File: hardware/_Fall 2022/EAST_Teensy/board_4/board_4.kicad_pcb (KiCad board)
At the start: 2 copper layers, 76.2 x 66.7 mm, 11 parts, among them J1 Conn_01x04, J2 Conn_02x09_Odd_Even, U1 Teensy4.1

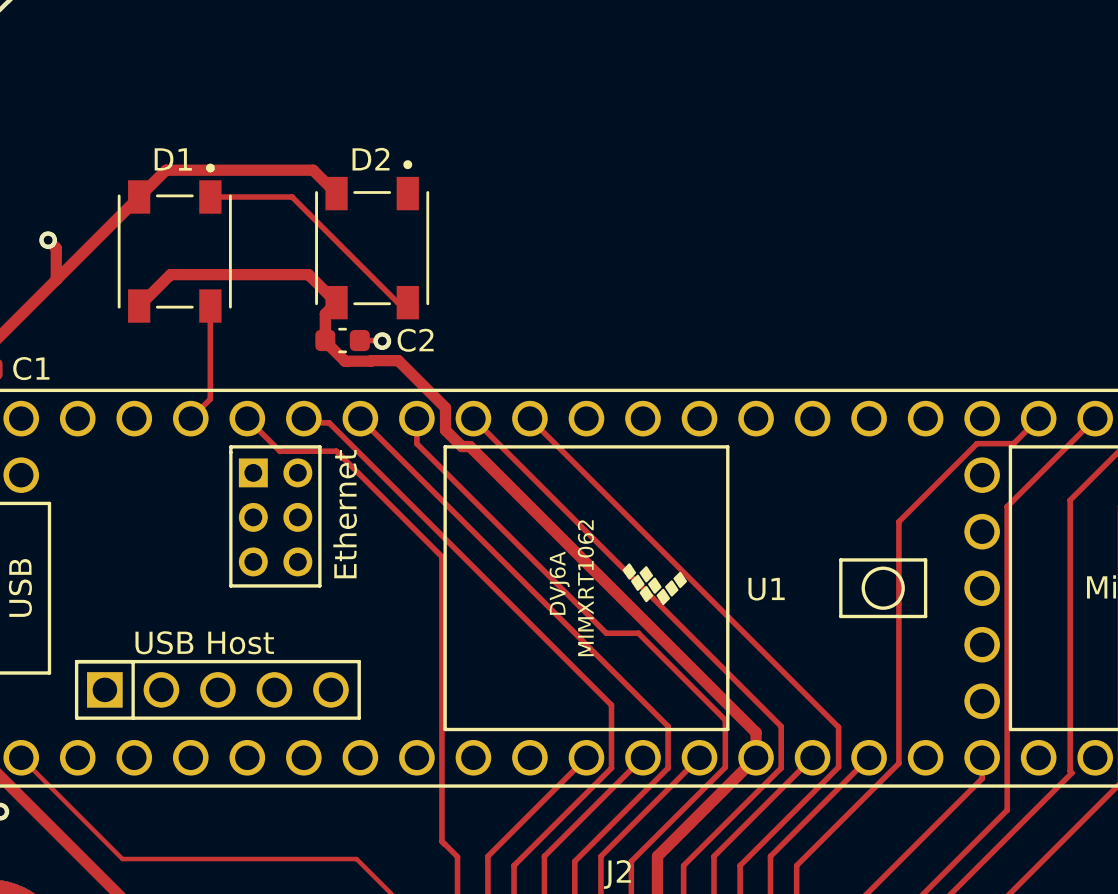
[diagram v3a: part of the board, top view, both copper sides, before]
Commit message: Edit for design rule check
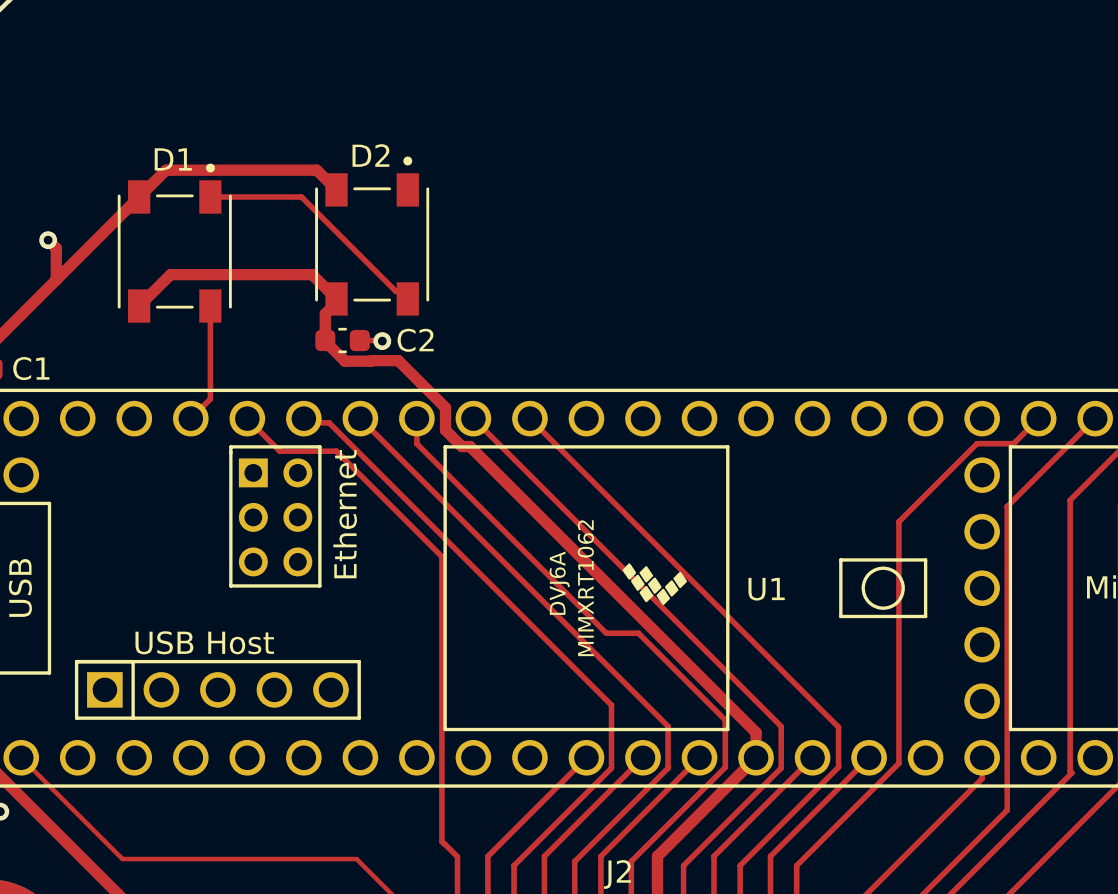
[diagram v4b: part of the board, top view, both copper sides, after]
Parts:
- moved D2 0.16 mm to (137.7, 107.2)
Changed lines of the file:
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@@
       (effects (font (size 1 1) (thickness 0.15)))
     )
-    (fp_text value "0.1uf" (at 0 1.43 180) (layer "F.Fab")
+    (fp_text value "0.1uf" (at 0 1.59495 180) (layer "F.Fab")
       (effects (font (size 1 1) (thickness 0.15)))
     )
@@
   )
   (footprint "Neopixel:LED_1655" (layer "F.Cu")
-    (at 137.72 107.3275 -90)
+    (at 137.72 107.16255 -90)
     (property "Sheetfile" "board_4.kicad_sch")
     (property "Sheetname" "")
@@
   (segment (start 137.84 140.68) (end 144.48 147.32) (width 0.508) (layer "F.Cu") (net 1))
   (segment (start 144.48 147.32) (end 161.798 147.32) (width 0.508) (layer "F.Cu") (net 1))
-  (segment (start 136.12 104.8775) (end 135.0685 103.826) (width 0.508) (layer "F.Cu") (net 2))
   (segment (start 123.525 107.335) (end 123.16 106.97) (width 0.508) (layer "F.Cu") (net 2))
+  (segment (start 135.23345 103.826) (end 136.12 104.71255) (width 0.508) (layer "F.Cu") (net 2))
   (segment (start 138.15 111.48) (end 138.176 111.506) (width 0.25) (layer "F.Cu") (net 2))
   (segment (start 137.84 138.14) (end 134.6 138.14) (width 0.508) (layer "F.Cu") (net 2))
-  (segment (start 128.454 103.826) (end 127.25 105.03) (width 0.508) (layer "F.Cu") (net 2))
   (segment (start 119.41 130.23) (end 119.41 131.05) (width 0.381) (layer "F.Cu") (net 2))
   (segment (start 134.6 138.14) (end 134.32 137.86) (width 0.508) (layer "F.Cu") (net 2))
   (segment (start 120.589 111.691) (end 120.589 112.845526) (width 0.508) (layer "F.Cu") (net 2))
-  (segment (start 135.0685 103.826) (end 128.454 103.826) (width 0.508) (layer "F.Cu") (net 2))
+  (segment (start 127.25 105.03) (end 128.454 103.826) (width 0.508) (layer "F.Cu") (net 2))
   (segment (start 123.525 108.755) (end 120.589 111.691) (width 0.508) (layer "F.Cu") (net 2))
   (segment (start 127.25 105.03) (end 123.525 108.755) (width 0.508) (layer "F.Cu") (net 2))
   (segment (start 137.165 111.48) (end 138.15 111.48) (width 0.25) (layer "F.Cu") (net 2))
   (segment (start 119.41 131.05) (end 121.01 132.65) (width 0.381) (layer "F.Cu") (net 2))
+  (segment (start 128.454 103.826) (end 135.23345 103.826) (width 0.508) (layer "F.Cu") (net 2))
   (segment (start 123.525 108.755) (end 123.525 107.335) (width 0.508) (layer "F.Cu") (net 2))
   (via (at 134.32 137.86) (size 0.8) (drill 0.4) (layers "F.Cu" "B.Cu") (net 2))
@@
   (via (at 138.176 111.506) (size 0.8) (drill 0.4) (layers "F.Cu" "B.Cu") (net 2))
   (via (at 123.16 106.97) (size 0.8) (drill 0.4) (layers "F.Cu" "B.Cu") (net 2))
-  (segment (start 130.45 105.03) (end 134.12 105.03) (width 0.25) (layer "F.Cu") (net 3))
-  (segment (start 134.12 105.03) (end 138.8675 109.7775) (width 0.25) (layer "F.Cu") (net 3))
-  (segment (start 138.8675 109.7775) (end 139.32 109.7775) (width 0.25) (layer "F.Cu") (net 3))
+  (segment (start 138.97825 109.2708) (end 139.32 109.61255) (width 0.25) (layer "F.Cu") (net 3))
+  (segment (start 130.45 105.03) (end 134.5448 105.03) (width 0.25) (layer "F.Cu") (net 3))
+  (segment (start 134.5448 105.03) (end 138.7856 109.2708) (width 0.25) (layer "F.Cu") (net 3))
+  (segment (start 138.7856 109.2708) (end 138.97825 109.2708) (width 0.25) (layer "F.Cu") (net 3))
   (segment (start 175.29 114.99) (end 171.3484 118.9316) (width 0.25) (layer "F.Cu") (net 4))
   (segment (start 171.3484 131.3688) (end 162.29 140.4272) (width 0.25) (layer "F.Cu") (net 4))
@@
   (segment (start 161.365 138.7106) (end 161.365 142.2014) (width 0.25) (layer "F.Cu") (net 5))
   (segment (start 169.164 130.9116) (end 161.365 138.7106) (width 0.25) (layer "F.Cu") (net 5))
-  (segment (start 134.862 108.5195) (end 128.6605 108.5195) (width 0.508) (layer "F.Cu") (net 6))
   (segment (start 137.671251 112.409) (end 136.501 112.409) (width 0.508) (layer "F.Cu") (net 6))
-  (segment (start 136.12 109.7775) (end 134.862 108.5195) (width 0.508) (layer "F.Cu") (net 6))
+  (segment (start 135.02695 108.5195) (end 136.12 109.61255) (width 0.508) (layer "F.Cu") (net 6))
   (segment (start 141.750576 116.244) (end 141.016 115.509424) (width 0.508) (layer "F.Cu") (net 6))
   (segment (start 150.54 138.14) (end 150.54 134.66) (width 0.508) (layer "F.Cu") (net 6))
   (segment (start 138.897424 112.384) (end 137.696251 112.384) (width 0.508) (layer "F.Cu") (net 6))
+  (segment (start 127.25 109.93) (end 128.6605 108.5195) (width 0.508) (layer "F.Cu") (net 6))
   (segment (start 141.016 114.502576) (end 138.897424 112.384) (width 0.508) (layer "F.Cu") (net 6))
   (segment (start 154.97 129.09863) (end 142.11537 116.244) (width 0.508) (layer "F.Cu") (net 6))
+  (segment (start 128.6605 108.5195) (end 135.02695 108.5195) (width 0.508) (layer "F.Cu") (net 6))
   (segment (start 154.97 130.23) (end 154.97 129.09863) (width 0.508) (layer "F.Cu") (net 6))
+  (segment (start 136.12 109.61255) (end 136.12 109.7775) (width 0.508) (layer "F.Cu") (net 6))
   (segment (start 142.11537 116.244) (end 141.750576 116.244) (width 0.508) (layer "F.Cu") (net 6))
   (segment (start 136.501 112.409) (end 135.615 111.523) (width 0.508) (layer "F.Cu") (net 6))
-  (segment (start 128.6605 108.5195) (end 127.25 109.93) (width 0.508) (layer "F.Cu") (net 6))
   (segment (start 141.016 115.509424) (end 141.016 114.502576) (width 0.508) (layer "F.Cu") (net 6))
   (segment (start 150.54 134.66) (end 154.97 130.23) (width 0.508) (layer "F.Cu") (net 6))
@@
   (segment (start 158.16 138.14) (end 165.13 131.17) (width 0.25) (layer "F.Cu") (net 9))
   (segment (start 165.13 131.17) (end 165.13 130.23) (width 0.25) (layer "F.Cu") (net 9))
-  (segment (start 164.64 130.23) (end 165.13 130.23) (width 0.25) (layer "F.Cu") (net 9))
   (segment (start 126.5 134.78) (end 137.02 134.78) (width 0.2032) (layer "F.Cu") (net 10))
   (segment (start 137.02 134.78) (end 140.38 138.14) (width 0.2032) (layer "F.Cu") (net 10))

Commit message: EAST JLC files
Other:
- board text added: "Ari Bobesh Charlie Babe Jiayuan Liu Lili Baker Rowan Jansens"
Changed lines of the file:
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@@
       (outputformat 1)
       (mirror false)
-      (drillshape 1)
+      (drillshape 0)
       (scaleselection 1)
-      (outputdirectory "")
+      (outputdirectory "JLC/")
     )
   )
@@
     (tags "mounting hole 3.7mm")
     (attr exclude_from_pos_files exclude_from_bom)
-    (fp_text reference "REF**" (at 10.414 1.27) (layer "F.SilkS")
+    (fp_text reference "REF**" (at 10.414 1.27) (layer "F.SilkS") hide
       (effects (font (size 1 1) (thickness 0.15)))
     )
@@
     (tags "mounting hole 3.7mm")
     (attr exclude_from_pos_files exclude_from_bom)
-    (fp_text reference "REF**" (at -0.656228 -9.486125) (layer "F.SilkS")
+    (fp_text reference "REF**" (at -0.656228 -9.486125) (layer "F.SilkS") hide
       (effects (font (size 1 1) (thickness 0.15)))
     )
@@
     (tags "mounting hole 3.7mm")
     (attr exclude_from_pos_files exclude_from_bom)
-    (fp_text reference "REF**" (at -9.228277 3.101257) (layer "F.SilkS")
+    (fp_text reference "REF**" (at -9.228277 3.101257) (layer "F.SilkS") hide
       (effects (font (size 1 1) (thickness 0.15)))
     )
@@
     (fp_line (start 0.5 1.375) (end 0 0.875) (layer "F.Fab") (width 0.1))
     (fp_line (start 7.25 0.25) (end -1.25 0.25) (layer "F.Fab") (width 0.1))
-    (pad "1" thru_hole roundrect (at 0 0) (size 1.2 1.75) (drill 0.75) (layers *.Cu *.Mask) (roundrect_rratio 0.208333)
+    (pad "1" thru_hole roundrect (at 0 0) (size 1.2 1.75) (drill 0.75) (layers *.Cu *.Mask) (roundrect_rratio 0.2083333333)
       (net 5 "/TX 0") (pinfunction "Pin_1") (pintype "passive"))
     (pad "2" thru_hole oval (at 2 0) (size 1.2 1.75) (drill 0.75) (layers *.Cu *.Mask)
@@
   (gr_line (start 122.779619 152.0952) (end 173.181181 152.0952) (layer "Edge.Cuts") (width 0.2))
   (gr_arc (start 122.779619 152.0952) (mid 147.9804 85.403268) (end 173.181181 152.0952) (layer "Edge.Cuts") (width 0.2))
+  (gr_text "Ari Bobesh\nCharlie Babe\nJiayuan Liu\nLili Baker\nRowan Jansens" (at 147.8788 104.4956) (layer "B.SilkS")
+    (effects (font (size 2 2) (thickness 0.15)) (justify mirror))
+  )
   (segment (start 137.84 140.68) (end 130.626576 140.68) (width 0.508) (layer "F.Cu") (net 1))
   (segment (start 120.671646 125.972938) (end 118.85 124.151292) (width 0.508) (layer "F.Cu") (net 1))

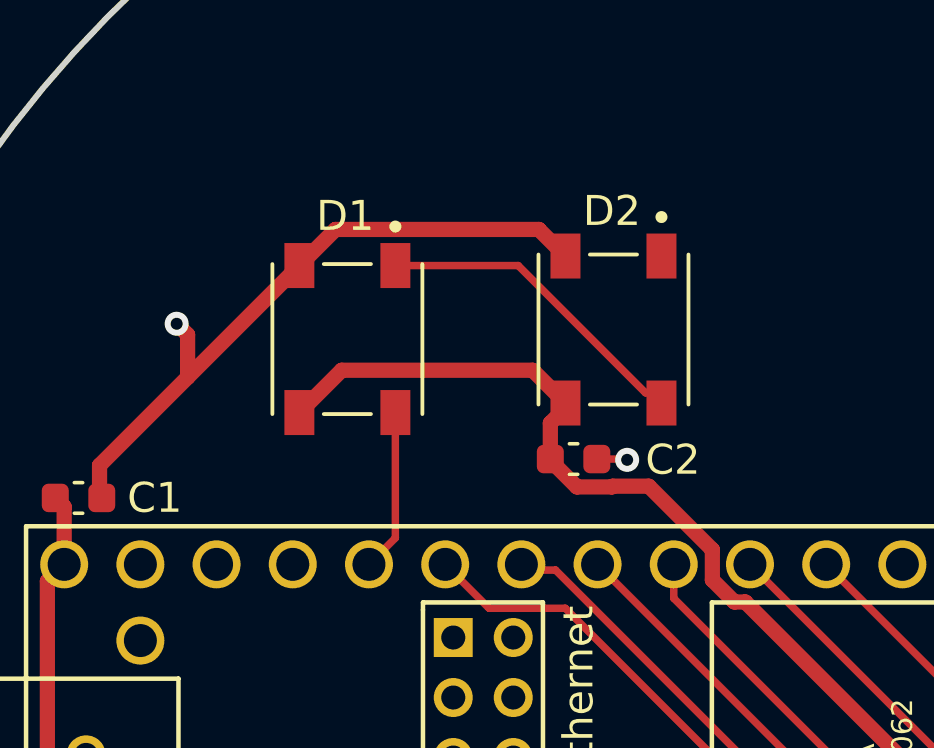
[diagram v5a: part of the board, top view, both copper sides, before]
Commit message: Changed neopixel on board 4
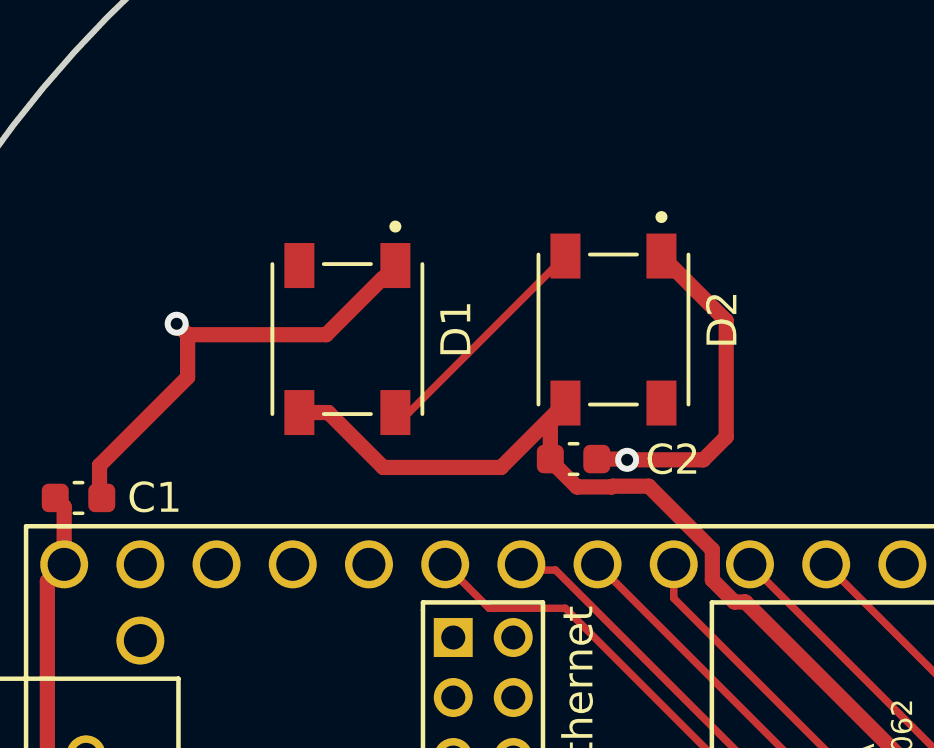
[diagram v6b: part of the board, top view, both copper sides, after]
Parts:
- D1: value Neopixel1 -> 1655; footprint Neopixel:LED_1655 -> neopixel:LED_1655
- D2: value Neopixel2 -> 1655; footprint Neopixel:LED_1655 -> neopixel:LED_1655
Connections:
- D1 pad 1: Net-(D1-Pad1) -> GND
- D1 pad 2: GND -> unconnected-(D1-Pad2)
- D1 pad 4: /NEOPIXEL -> Net-(D1-Pad4)
- D2 pad 1: unconnected-(D2-Pad1) -> GND
- D2 pad 2: GND -> Net-(D1-Pad4)
- D2 pad 4: Net-(D1-Pad1) -> unconnected-(D2-Pad4)
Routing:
- net Net-(D1-Pad1): track 10.8 -> 0.00 mm
- net Net-(D1-Pad4): track 0.00 -> 7.83 mm
- net /NEOPIXEL: track 5.42 -> 0.00 mm
- net GND: track 30.0 -> 32.8 mm
- net /3.3V: track 50.1 -> 50.8 mm

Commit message: pcb fixes
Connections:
- net /MISO 1 renamed /MISO
- net /MOSI 1 renamed /MOSI
- net /RX 0 renamed /RX 8
- net /RX 1 renamed /RX 4
- net /RX 2 renamed /RX 5
- net /TX 0 renamed /TX 8
- net /TX 1 renamed /TX 4
- net /TX 2 renamed /TX 5
- D1 pad 2: unconnected-(D1-Pad2) -> /NEOPIXEL
- J2 pad 18: /SCK 1 -> /SCK
- U1 pad 19: /SCK 1 -> unconnected-(U1-Pad19)
- U1 pad 35: unconnected-(U1-Pad35) -> /SCK
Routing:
- net /SCK: track 0.00 -> 30.3 mm, vias 0 -> 2
- net GND: track 32.8 -> 20.5 mm, vias 4 -> 2
- net /NEOPIXEL: track 0.00 -> 12.3 mm
- net /SCK 1: track 10.8 -> 0.00 mm
- net /V_BATT: track 69.3 -> 73.2 mm
- net /3.3V: track 50.8 -> 48.7 mm
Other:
- board text added: "3.3"
- board text added: "CS1"
- board text added: "CS2"
- board text added: "CS3"
- board text added: "CS4"
- board text added: "GND"
- board text added: "MISO"
- board text added: "MOSI"
- board text added: "RX1"
- board text added: "RX2"
- board text added: "SCK"
- board text added: "SCL1"
- board text added: "SCL2"
- board text added: "SDA1"
- board text added: "SDA2"
- board text added: "TX1"
- board text added: "TX2"
- board text added: "VBAT"

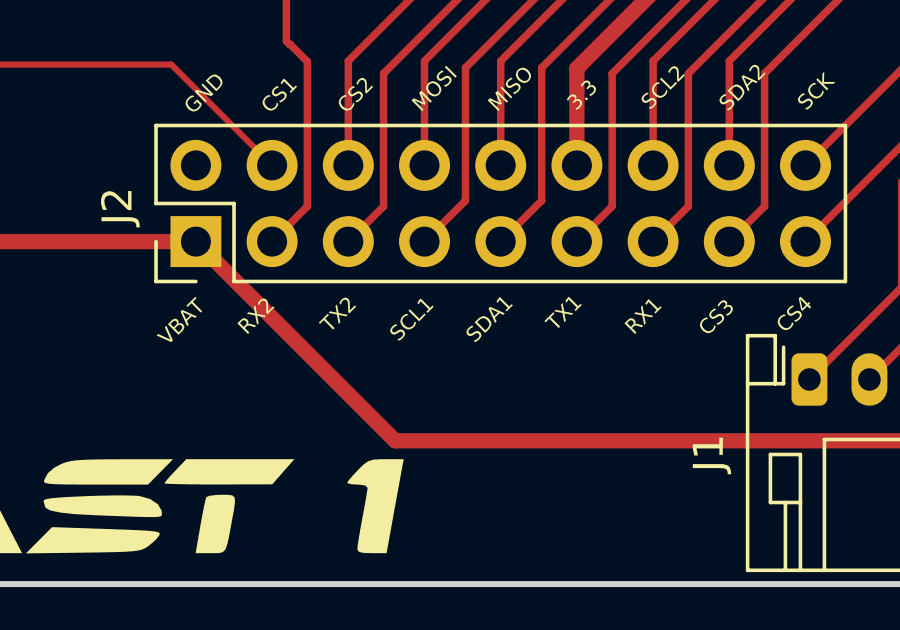
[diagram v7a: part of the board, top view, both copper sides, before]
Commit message: fixed a few pcb silkscreen things
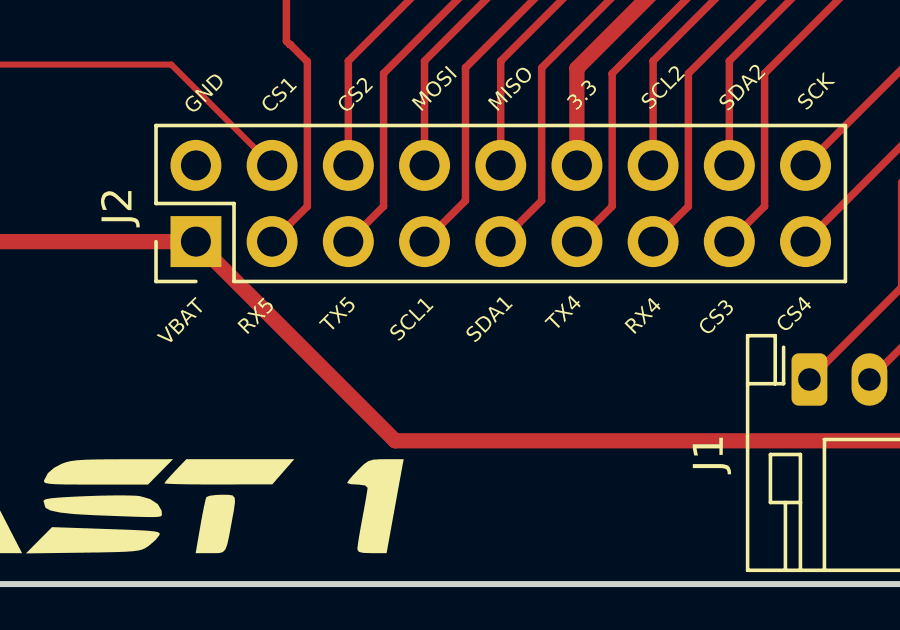
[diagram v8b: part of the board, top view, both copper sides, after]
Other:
- board text added: "RX4"
- board text added: "RX5"
- board text added: "TX4"
- board text added: "TX5"
- board text removed: "RX1"
- board text removed: "RX2"
- board text removed: "TX1"
- board text removed: "TX2"
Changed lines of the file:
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@@
     (effects (font (size 0.5 0.5) (thickness 0.125)))
   )
-  (gr_text "TX1" (at 150.114 143.0528 45) (layer "F.SilkS")
+  (gr_text "TX4" (at 150.114 143.0528 45) (layer "F.SilkS")
     (effects (font (size 0.5 0.5) (thickness 0.125)))
   )
-  (gr_text "RX1" (at 152.7556 143.1544 45) (layer "F.SilkS")
+  (gr_text "RX4" (at 152.7556 143.1544 45) (layer "F.SilkS")
     (effects (font (size 0.5 0.5) (thickness 0.125)))
   )
@@
     (effects (font (size 0.5 0.5) (thickness 0.125)))
   )
-  (gr_text "RX2" (at 139.8524 143.1544 45) (layer "F.SilkS")
+  (gr_text "RX5" (at 139.8524 143.1544 45) (layer "F.SilkS")
     (effects (font (size 0.5 0.5) (thickness 0.125)))
   )
@@
     (effects (font (size 0.5 0.5) (thickness 0.125)))
   )
-  (gr_text "TX2" (at 142.5956 143.1036 45) (layer "F.SilkS")
+  (gr_text "TX5" (at 142.5956 143.1036 45) (layer "F.SilkS")
     (effects (font (size 0.5 0.5) (thickness 0.125)))
   )
